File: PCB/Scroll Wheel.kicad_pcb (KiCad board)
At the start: 2 copper layers, 44.8 x 60.3 mm, 37 parts, among them J1 TC2030, J2 USB_C_Receptacle_USB3.0_12P, J3 Battery, J4 Conn_01x04_Socket, J5 Conn_01x04_Pin, Q1 FS8205A, SW1 SW_Nidec_CAS-120A1, U1 ESP32-WROOM-E, U2 HUSB238, U3 SI4459ADY-T1-GE3, U4 TP4056-42-ESOP8, U5 DW01A, U6 MIC5504-3.3YM5, U7 AS5600

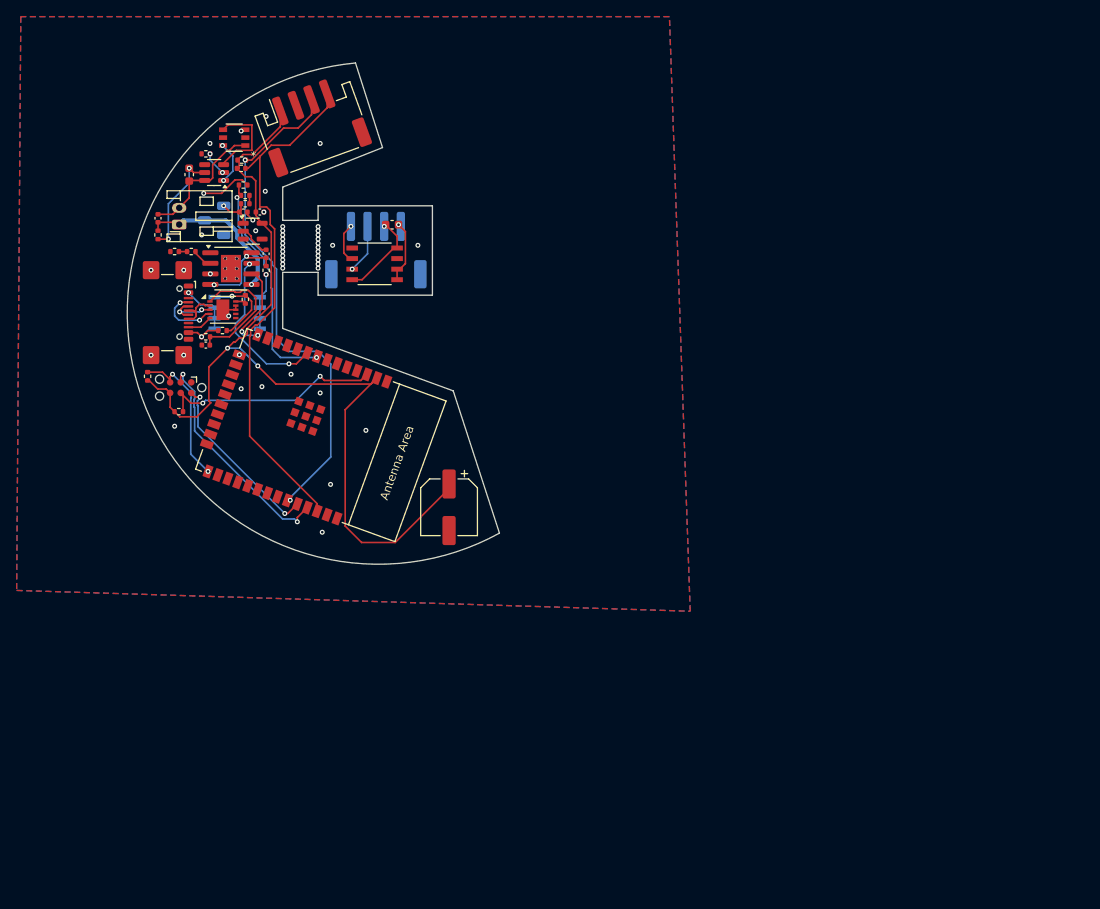
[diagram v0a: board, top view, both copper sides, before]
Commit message: Battery Part Redesign
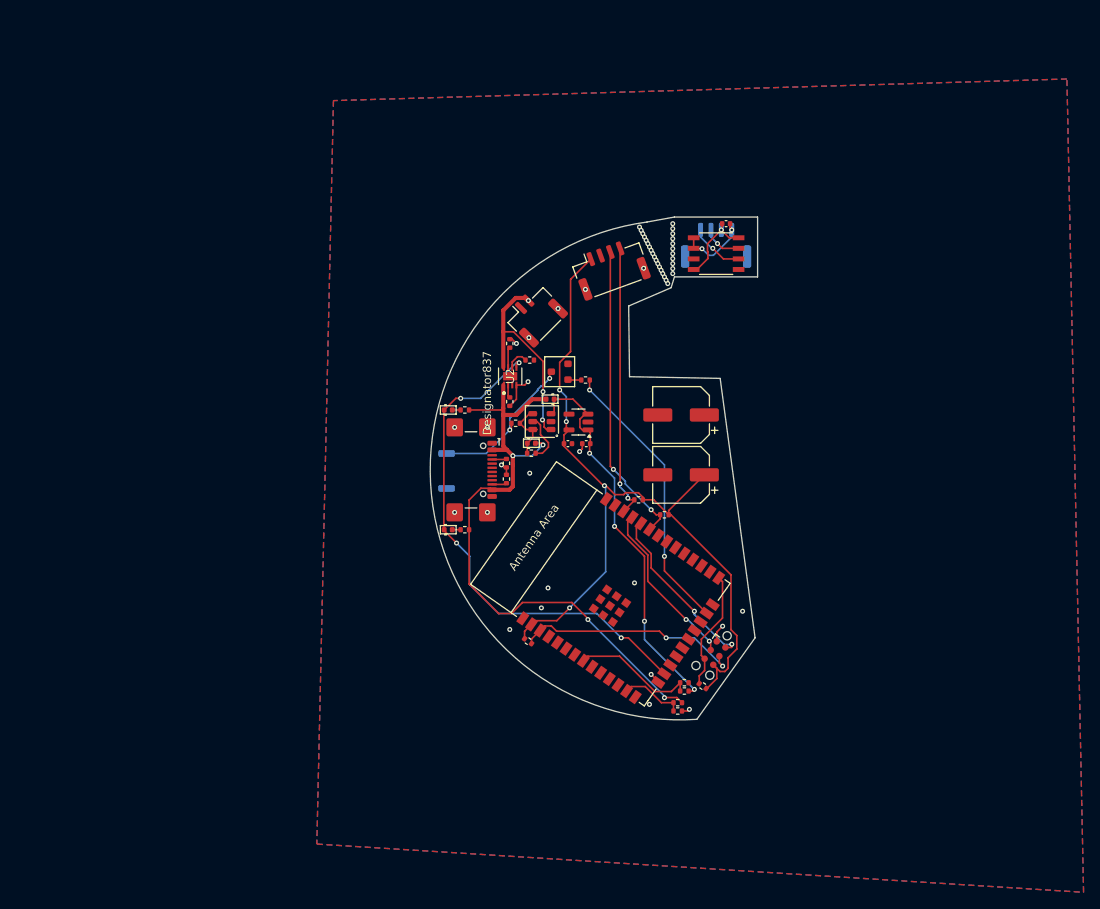
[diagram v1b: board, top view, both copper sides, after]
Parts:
- removed C1: 1uF, Capacitor_SMD:C_0402_1005Metric
- removed C6: 10uF, Capacitor_SMD:C_0402_1005Metric
- removed C8: 0.1uF, Capacitor_SMD:C_0603_1608Metric
- removed R10: 100, Resistor_SMD:R_0402_1005Metric
- removed R2: 10, Resistor_SMD:R_0402_1005Metric
- removed R3: 49.9k, Resistor_SMD:R_0402_1005Metric
- removed R4: 5.1k, Resistor_SMD:R_0402_1005Metric
- removed R5: 0,4, Resistor_SMD:R_0402_1005Metric
- removed U3: SI4459ADY-T1-GE3, footprints:SO_ADY-T1-GE3_VIS
- removed U4: TP4056-42-ESOP8, Package_SO:SOIC-8-1EP_3.9x4.9mm_P1.27mm_EP2.41x3.3mm_ThermalVias
- removed U5: DW01A, Package_TO_SOT_SMD:SOT-23-6
- added D1: LED, PCM_Diode_SMD_AKL:D_0402_1005Metric, F.Cu at (98.4, 64.8)
- added D3: D, PCM_Diode_SMD_AKL:D_0402_1005Metric, F.Cu at (110.7, 63.5)
- added D4: LED, PCM_Diode_SMD_AKL:D_0402_1005Metric, F.Cu at (98.4, 79.2)
- added D5: D, PCM_Diode_SMD_AKL:D_0402_1005Metric, F.Cu at (108.4, 68.8)
- added Q2: BC847, PCM_Package_TO_SOT_SMD_AKL:SOT-23, F.Cu at (111.8, 60.2)
- added R21: 5.1k, Resistor_SMD:R_0402_1005Metric, F.Cu at (105.4, 73.1)
- added R22: 5.1k, Resistor_SMD:R_0402_1005Metric, F.Cu at (105.4, 71.2)
- added R24: 5.1k, Resistor_SMD:R_0402_1005Metric, F.Cu at (126.0, 101.0)
- added R25: 1k, Resistor_SMD:R_0402_1005Metric, F.Cu at (100.4, 79.2)
- added R26: 5.1k, Resistor_SMD:R_0402_1005Metric, F.Cu at (106.5, 66.4)
- added R28: 5.1k, Resistor_SMD:R_0402_1005Metric, F.Cu at (114.9, 61.2)
- added R30: 1M, Resistor_SMD:R_0402_1005Metric, F.Cu at (108.4, 70.0)
- added R8: 2.7k, Resistor_SMD:R_0402_1005Metric, F.Cu at (126.8, 98.6)
- C10, C9: value 1uF -> 22uF
- C11: value 100nF -> 22uF; footprint Capacitor_SMD:C_0603_1608Metric -> Capacitor_SMD:C_0402_1005Metric
- C7: value 10uF -> 100uF; footprint Capacitor_SMD:C_0402_1005Metric -> Capacitor_SMD:CP_Elec_6.3x5.4
- J2: value USB_C_Receptacle_USB3.0_12P -> USB_C_Receptacle_USB3.1_16P
- J3: value Battery -> Conn_01x02_Pin; footprint Connector_JST:JST_PH_S2B-PH-K_1x02_P2.00mm_Horizontal -> Connector_JST:JST_GH_SM02B-GHS-TB_1x02-1MP_P1.25mm_Horizontal
- J4, J5: footprint Connector_JST:JST_PH_S4B-PH-SM4-TB_1x04-1MP_P2.00mm_Horizontal -> Connector_JST:JST_GH_SM04B-GHS-TB_1x04-1MP_P1.25mm_Horizontal
- Q1: footprint footprints:SOT-23-6L_TCP -> PCM_Package_TO_SOT_SMD_AKL:SOT-23-6
- R12: value 8.2k -> 5.1k
- R17: value 5.1k -> 330
- R18: value 5.1k -> 24k
- R19: value 5.1k -> 1k
- R20: value 5.1k -> 27k
- R9: value 1k -> 2.7k
- SW1: value SW_Nidec_CAS-120A1 -> SW_Push; footprint Button_Switch_SMD:Nidec_Copal_CAS-120A -> Button_Switch_SMD:SW_Push_SPST_NO_Alps_SKRK
- U2: value HUSB238 -> BQ25172DSGR; footprint Package_DFN_QFN:DFN-10-1EP_3x3mm_P0.5mm_EP1.55x2.48mm -> BQ25172:DSG0008A-IPC_A
- U7: footprint footprints:AS5600 -> AS5600:AS5600
- moved R9 87.0 mm to (126.0, 100.0), turned to 0 degrees
- moved R12 80.0 mm to (126.8, 97.6)
- moved R14 76.4 mm to (129.0, 98.0), turned to 145 degrees
- moved J1 71.7 mm to (130.5, 94.0), turned to -125 degrees
- moved C7 67.2 mm to (126.4, 65.4), turned to 180 degrees
- moved R16 66.4 mm to (124.4, 77.4), turned to 0 degrees
- moved R15 62.2 mm to (121.3, 75.6), turned to 0 degrees
- moved Q1 50.4 mm to (109.7, 66.2)
- moved R13 50.3 mm to (108.0, 92.6), turned to 145 degrees
- moved C9 49.8 mm to (115.0, 68.8), turned to 0 degrees
- moved C10 46.4 mm to (112.8, 68.8)
- moved U6 45.4 mm to (114.1, 66.2), turned to 180 degrees
- moved J3 44.2 mm to (108.9, 53.4), turned to 45 degrees
- moved R17 42.3 mm to (105.8, 63.8), turned to 90 degrees
- moved R18 41.8 mm to (105.8, 56.8), turned to -90 degrees
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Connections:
- C7 pad 1: BATT_gnd -> +5V
- C7 pad 2: BATT -> GND
- C9 pad 2: Net-(SW1-C) -> Net-(D3-K)
- J2 pad A4: VBUS -> VDC
- J2 pad A5: CC1 -> Net-(J2-CC1)
- J2 pad A6: D+ -> unconnected-(J2-D+-PadA6)
- J2 pad A7: D- -> unconnected-(J2-D--PadA7)
- J2 pad A9: VBUS -> VDC
- J2 pad B4: VBUS -> VDC
- J2 pad B5: CC2 -> Net-(J2-CC2)
- J2 pad B6: D+ -> unconnected-(J2-D+-PadB6)
- J2 pad B7: D- -> unconnected-(J2-D--PadB7)
- J2 pad B9: VBUS -> VDC
- J3 pad 1: BATT -> GND
- J3 pad 2: BATT_gnd -> BATT
- Q1 pad 1: BATT_gnd -> BATT
- Q1 pad 3: GND -> Net-(D3-K)
- Q1 pad 4: Net-(U5-OC) -> Net-(D5-K)
- Q1 pad 5: unconnected-(Q1-Pad5) -> Net-(Q1-Pad5)
- Q1 pad 6: Net-(U5-OD) -> Net-(D5-K)
- R17 pad 1: Net-(U4-PROG) -> GND
- R17 pad 2: Net-(R17-Pad2) -> Net-(U2-ISET)
- R18 pad 1: Net-(R17-Pad2) -> GND
- R18 pad 2: GND -> Net-(U2-VSET)
- R19 pad 1: Net-(R19-Pad1) -> Net-(D1-A)
- R19 pad 2: Net-(SW1-C) -> VDC
- R20 pad 1: BATT_sense -> Net-(U2-TMR)
- R20 pad 2: Net-(R19-Pad1) -> GND
- R9 pad 1: Net-(U5-CS) -> PWR_sense
- R9 pad 2: GND -> VDC
- SW1 pad 1: Net-(SW1-C) -> GND
- SW1 pad 2: BATT -> Net-(Q2-C)
- U1 pad 13: unconnected-(U1-MTMS/GPIO14/ADC2_CH6-Pad13) -> PWR_sense
- U1 pad 16: unconnected-(U1-MTCK/GPIO13/ADC2_CH4-Pad16) -> STATE
- U1 pad 23: unconnected-(U1-MTDO/GPIO15/ADC2_CH3-Pad23) -> PWR_sw
- U2 pad 1: Net-(U2-VIN) -> VDC
- U2 pad 2: D+ -> Net-(U2-ISET)
- U2 pad 3: D- -> unconnected-(U2-TS-Pad3)
- U2 pad 4: CC1 -> GND
- U2 pad 5: CC2 -> STATE
- U2 pad 6: unconnected-(U2-SDA-Pad6) -> Net-(U2-TMR)
- U2 pad 7: unconnected-(U2-SCL-Pad7) -> Net-(U2-VSET)
- U2 pad 8: GND -> BATT
- U6 pad 1: Net-(SW1-C) -> Net-(D3-K)
- U6 pad 3: unconnected-(U6-EN-Pad3) -> Net-(D3-K)
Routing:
- net VDC: track 0.00 -> 78.8 mm, vias 0 -> 4
- net STATE: track 0.00 -> 62.5 mm, vias 0 -> 4
- net Net-(D3-K): track 0.00 -> 47.8 mm, vias 0 -> 4
- net PWR_sw: track 0.00 -> 33.9 mm, vias 0 -> 2
- net SDA: track 63.1 -> 33.2 mm, vias 0 -> 2
- net SCL: track 61.5 -> 36.7 mm
- net CHRG: track 20.0 -> 0.00 mm, vias 2 -> 0
- net Net-(Q2-C): track 0.00 -> 18.8 mm, vias 0 -> 2
- net BATT_gnd: track 16.0 -> 0.00 mm
- net Net-(U2-VIN): track 15.9 -> 0.00 mm
- net VBUS: track 12.9 -> 0.00 mm, vias 2 -> 0
- net Net-(U5-VCC): track 12.9 -> 0.00 mm, vias 2 -> 0
- net BATT_sense: track 27.7 -> 15.1 mm, vias 2 -> 0
- net Net-(U5-OC): track 11.0 -> 0.00 mm
- net STDBY: track 10.9 -> 0.00 mm, vias 2 -> 0
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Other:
- board size 44.8 x 60.3 mm -> 39.4 x 60.5 mm
- board text added: "Mario Langhammer"
- board text added: "V2.2"
- board text added: "github.com/ Mallo321123/Scroll-Wheel"

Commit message: Finish CAD Model
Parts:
- removed Q1: FS8205A, PCM_Package_TO_SOT_SMD_AKL:SOT-23-6
- removed R30: 1M, Resistor_SMD:R_0402_1005Metric
- added Q3: FDC6318P, Package_TO_SOT_SMD:SOT-23-6, F.Cu at (109.7, 66.3)
- added R31: 1M, Resistor_SMD:R_0402_1005Metric, F.Cu at (106.8, 68.2)
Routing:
- net Net-(Q3A-S1): track 0.00 -> 9.29 mm, vias 0 -> 2
- net Net-(Q1-Pad5): track 6.00 -> 0.00 mm
- net Net-(D3-K): track 47.8 -> 51.0 mm, vias 4 -> 6
- net BATT: track 25.9 -> 23.8 mm
- net Net-(D5-K): track 8.45 -> 6.74 mm
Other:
- board text added: "V2.3"
- board text removed: "V2.2"

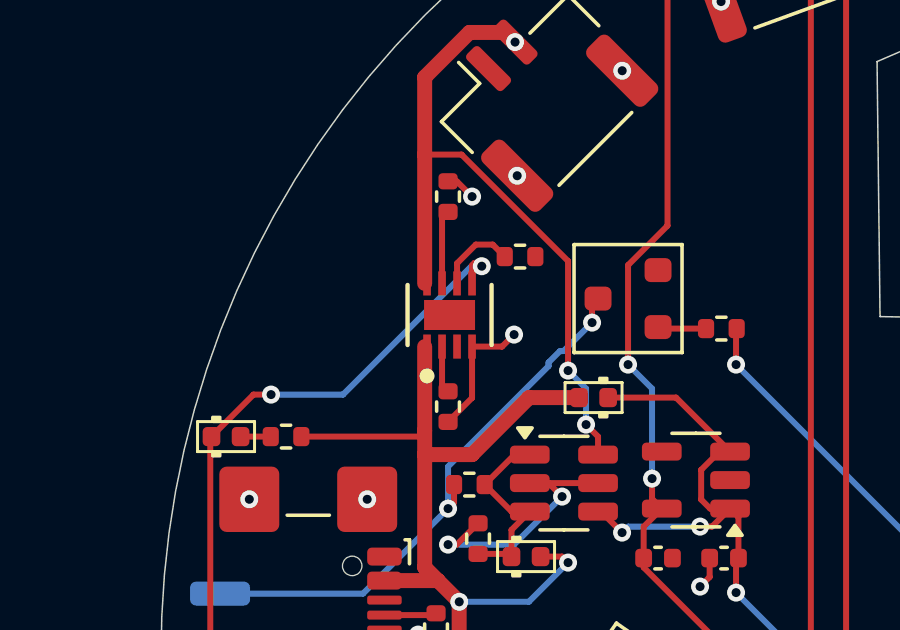
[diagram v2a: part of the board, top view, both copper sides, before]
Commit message: add missing label
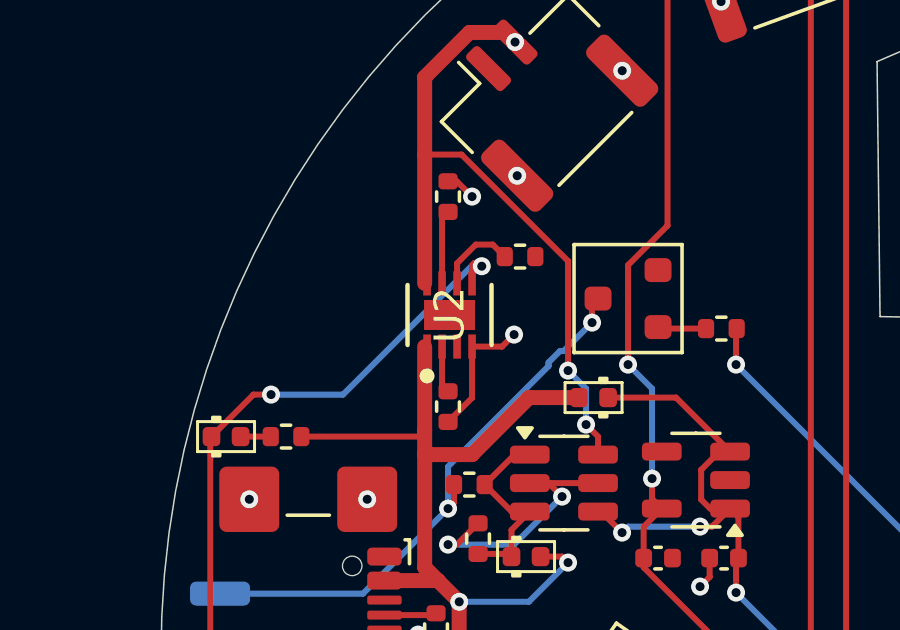
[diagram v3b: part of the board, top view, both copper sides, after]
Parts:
- J4: value Conn_01x04_Socket -> Connector Encoder
- J5: value Conn_01x04_Pin -> Connector controller
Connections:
- net Net-(D3-K) renamed BATT_sense_high
- C10 pad 1: GND -> Net-(U6-GND)
- C9 pad 1: GND -> Net-(U6-GND)
- U1 pad 14: STDBY -> unconnected-(U1-MTDI/GPIO12/ADC2_CH5-Pad14)
- U1 pad 34: RX -> unconnected-(U1-U0RXD/GPIO3-Pad34)
- U1 pad 9: CHRG -> unconnected-(U1-32K_XN/GPIO33/ADC1_CH5-Pad9)
- U6 pad 2: GND -> Net-(U6-GND)
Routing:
- net Net-(U6-GND): track 0.00 -> 1.08 mm, vias 0 -> 1
- net GND: track 12.5 -> 11.4 mm, vias 22 -> 21
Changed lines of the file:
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@@
 	)
 	(net 0 "")
-	(net 1 "Net-(D3-K)")
+	(net 1 "BATT_sense_high")
 	(net 2 "GND")
 	(net 3 "+5V")
@@
 	(net 20 "Net-(U2-ISET)")
 	(net 21 "Net-(U2-VSET)")
-	(net 22 "CHRG")
-	(net 23 "STDBY")
+	(net 22 "Net-(U6-GND)")
+	(net 23 "unconnected-(U1-MTDI{slash}GPIO12{slash}ADC2_CH5-Pad14)")
 	(net 24 "Net-(U2-TMR)")
 	(net 25 "BATT_sense")
@@
 	(net 55 "PWR_sw")
 	(net 56 "Net-(Q3A-S1)")
+	(net 57 "unconnected-(U1-32K_XN{slash}GPIO33{slash}ADC1_CH5-Pad9)")
+	(net 58 "unconnected-(U1-U0RXD{slash}GPIO3-Pad34)")
 	(footprint "Resistor_SMD:R_0402_1005Metric"
 		(layer "F.Cu")
@@
 			(layers "F.Cu" "F.Mask" "F.Paste")
 			(roundrect_rratio 0.25)
-			(net 1 "Net-(D3-K)")
+			(net 1 "BATT_sense_high")
 			(pintype "passive")
 		)
@@
 			(layers "F.Cu" "F.Mask" "F.Paste")
 			(roundrect_rratio 0.25)
-			(net 1 "Net-(D3-K)")
+			(net 1 "BATT_sense_high")
 			(pinfunction "VIN")
 			(pintype "power_in")
@@
 			(layers "F.Cu" "F.Mask" "F.Paste")
 			(roundrect_rratio 0.25)
-			(net 2 "GND")
+			(net 22 "Net-(U6-GND)")
 			(pinfunction "GND")
 			(pintype "power_in")
@@
 			(layers "F.Cu" "F.Mask" "F.Paste")
 			(roundrect_rratio 0.25)
-			(net 1 "Net-(D3-K)")
+			(net 1 "BATT_sense_high")
 			(pinfunction "EN")
 			(pintype "input")
@@
 			(layers "F.Cu" "F.Mask" "F.Paste")
 			(roundrect_rratio 0.25)
-			(net 2 "GND")
+			(net 22 "Net-(U6-GND)")
 			(pintype "passive")
 		)
@@
 			(layers "F.Cu" "F.Mask" "F.Paste")
 			(roundrect_rratio 0.25)
-			(net 1 "Net-(D3-K)")
+			(net 1 "BATT_sense_high")
 			(pintype "passive")
 		)
@@
 			(layers "F.Cu" "F.Mask" "F.Paste")
 			(roundrect_rratio 0.25)
-			(net 2 "GND")
+			(net 22 "Net-(U6-GND)")
 			(pintype "passive")
 		)
@@
 			(unlocked yes)
 			(layer "F.SilkS")
-			(hide yes)
 			(effects
 				(font
@@
 		)
 		(embedded_fonts no)
-		(model "${KIPRJMOD}/Librarys/3d/DSG0008A.stp"
-			(offset
-				(xyz 0 0 0)
-			)
-			(scale
-				(xyz 1 1 1)
-			)
-			(rotate
-				(xyz 0 0 0)
-			)
-		)
 	)
 	(footprint "Connector:Tag-Connect_TC2030-IDC-NL_2x03_P1.27mm_Vertical"
@@
 			(layers "F.Cu" "F.Mask" "F.Paste")
 			(roundrect_rratio 0.25)
-			(net 1 "Net-(D3-K)")
+			(net 1 "BATT_sense_high")
 			(pinfunction "D2")
 			(pintype "passive")
@@
 			)
 		)
-		(property "Value" "Conn_01x04_Pin"
+		(property "Value" "Connector controller"
 			(at 0 3.9 20)
 			(layer "F.Fab")
@@
 			(layers "F.Cu" "F.Mask" "F.Paste")
 			(roundrect_rratio 0.25)
-			(net 1 "Net-(D3-K)")
+			(net 1 "BATT_sense_high")
 			(pinfunction "K")
 			(pintype "passive")
@@
 			(size 1.5 0.9)
 			(layers "F.Cu" "F.Mask" "F.Paste")
-			(net 22 "CHRG")
+			(net 57 "unconnected-(U1-32K_XN{slash}GPIO33{slash}ADC1_CH5-Pad9)")
 			(pinfunction "32K_XN/GPIO33/ADC1_CH5")
 			(pintype "bidirectional")
@@
 			(size 1.5 0.9)
 			(layers "F.Cu" "F.Mask" "F.Paste")
-			(net 23 "STDBY")
+			(net 23 "unconnected-(U1-MTDI{slash}GPIO12{slash}ADC2_CH5-Pad14)")
 			(pinfunction "MTDI/GPIO12/ADC2_CH5")
 			(pintype "bidirectional")
@@
 			(size 1.5 0.9)
 			(layers "F.Cu" "F.Mask" "F.Paste")
-			(net 10 "RX")
+			(net 58 "unconnected-(U1-U0RXD{slash}GPIO3-Pad34)")
 			(pinfunction "U0RXD/GPIO3")
 			(pintype "bidirectional")
@@
 			)
 		)
-		(property "Value" "Conn_01x04_Socket"
+		(property "Value" "Connector Encoder"
 			(at 0 -3.9 0)
 			(layer "B.Fab")
@@
 	)
 	(segment
-		(start 114.52 68.85)
-		(end 114.52 69.48)
-		(width 0.2)
-		(layer "F.Cu")
-		(net 2)
-	)
-	(segment
 		(start 106.599999 61.8)
 		(end 107.6 61.8)
@@
 	)
 	(segment
-		(start 114.52 69.48)
-		(end 114.2 69.8)
-		(width 0.2)
-		(layer "F.Cu")
-		(net 2)
-	)
-	(segment
 		(start 105.8 64.31)
 		(end 106.599999 63.510001)
@@
 	)
 	(via
-		(at 114.2 69.8)
-		(size 0.6)
-		(drill 0.3)
-		(layers "F.Cu" "B.Cu")
-		(net 2)
-	)
-	(via
 		(at 108 61.4)
 		(size 0.6)
@@
 	)
 	(segment
+		(start 114.52 68.85)
+		(end 114.52 69.48)
+		(width 0.2)
+		(layer "F.Cu")
+		(net 22)
+	)
+	(segment
+		(start 114.52 69.48)
+		(end 114.2 69.8)
+		(width 0.2)
+		(layer "F.Cu")
+		(net 22)
+	)
+	(via
+		(at 114.2 69.8)
+		(size 0.6)
+		(drill 0.3)
+		(layers "F.Cu" "B.Cu")
+		(net 22)
+	)
+	(segment
